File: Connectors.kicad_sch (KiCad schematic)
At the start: 13 parts, among them J11 Micro_SD_Card_Det, J12 JST-PH, J13 USB_C_Receptacle_USB2.0, U10 USBLC6-2SC6

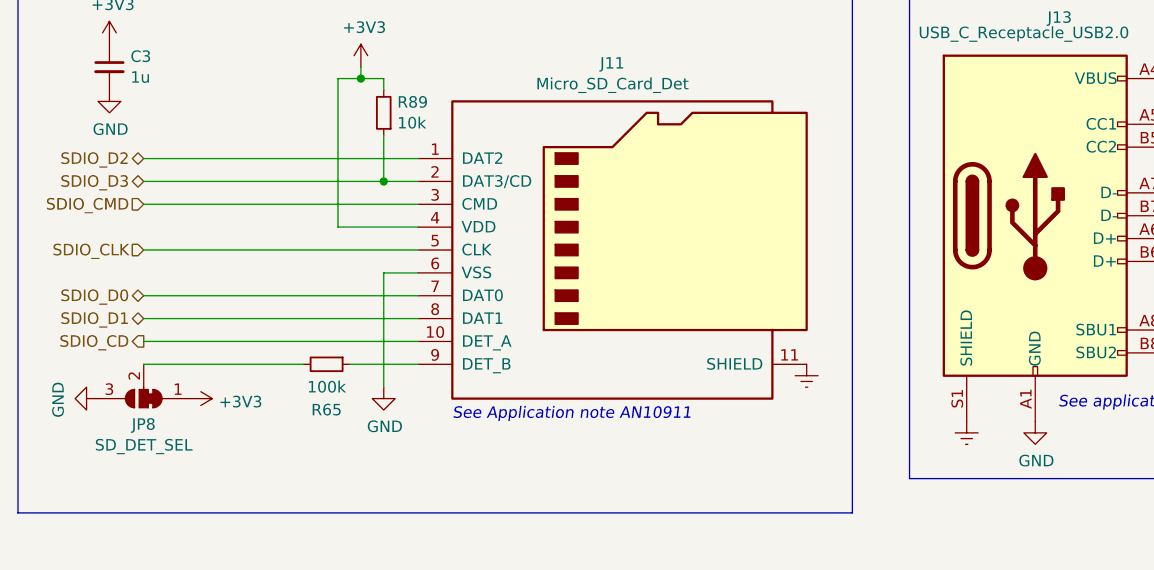
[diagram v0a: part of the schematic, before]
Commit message: (deps) upgrade to KiCad 7.0
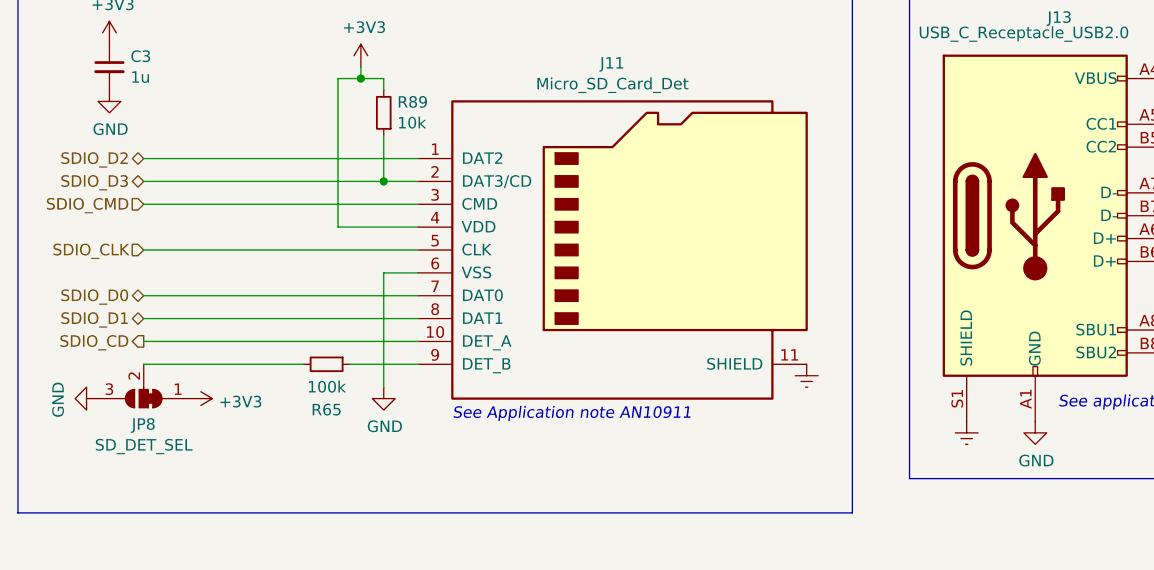
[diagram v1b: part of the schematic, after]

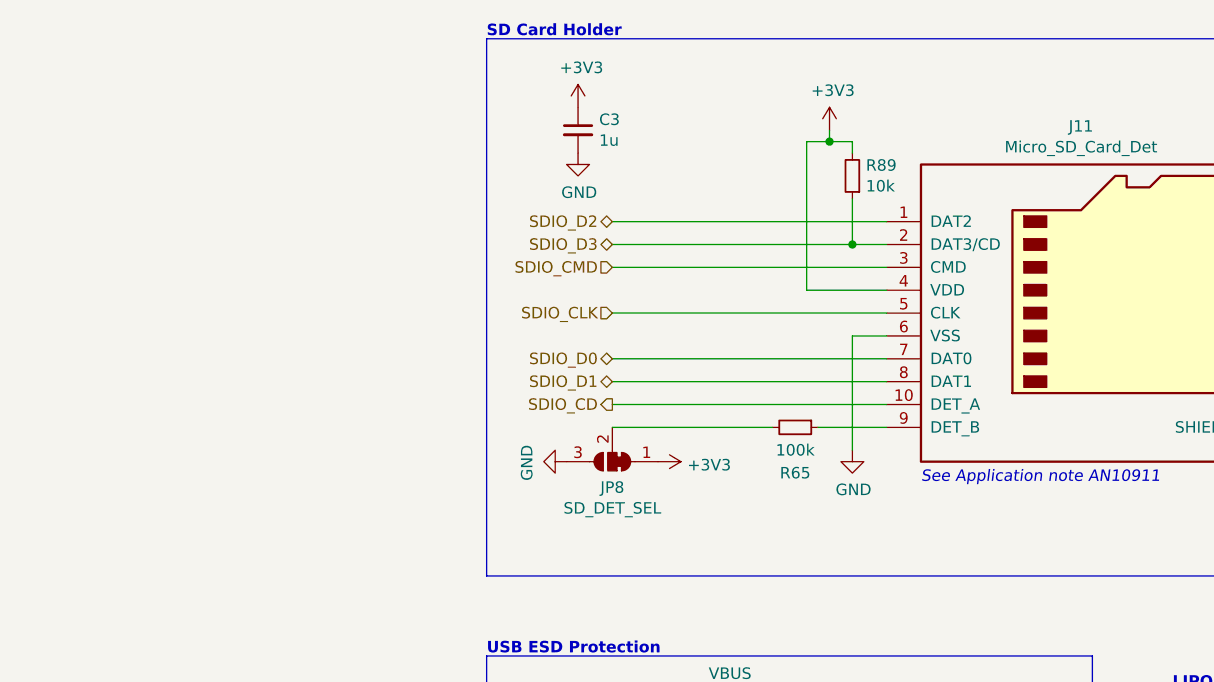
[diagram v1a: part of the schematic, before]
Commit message: (sch) update sd card interface
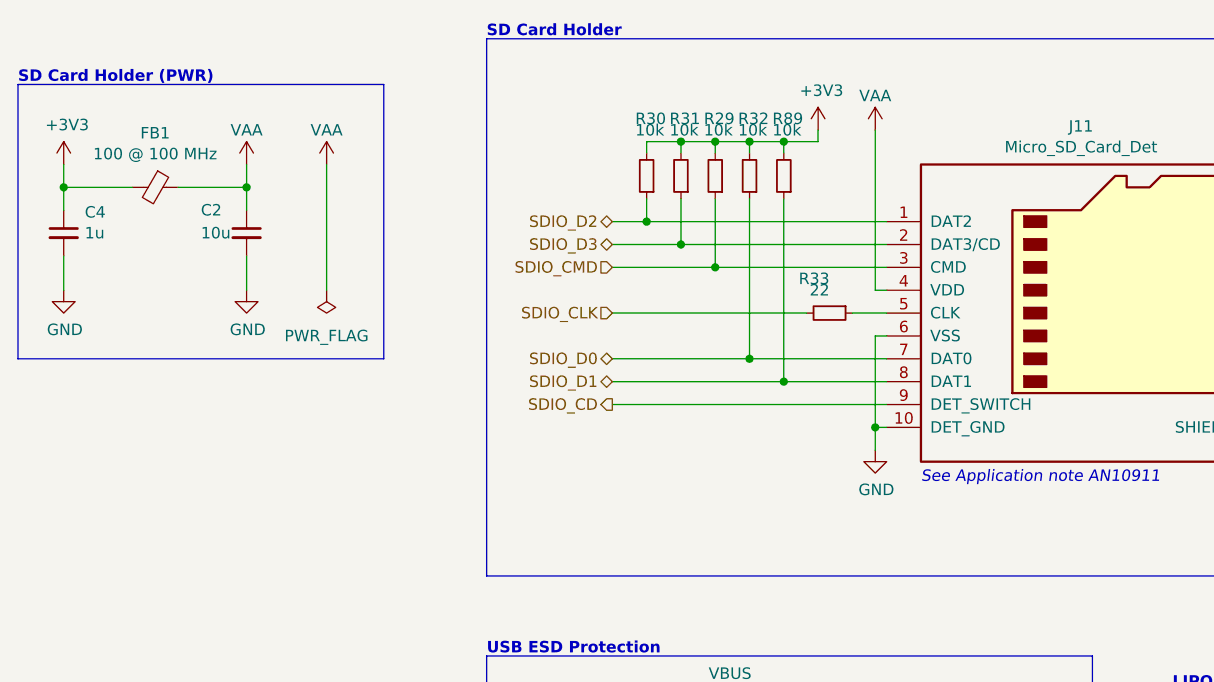
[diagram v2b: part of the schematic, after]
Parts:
- removed C3: 1u, Capacitor_SMD:C_0603_1608Metric_Pad1.08x0.95mm_HandSolder, symbol Device:C_Small
- removed JP8: SD_DET_SEL, Jumper:SolderJumper-3_P1.3mm_Bridged12_RoundedPad1.0x1.5mm_NumberLabels, symbol Jumper:SolderJumper_3_Bridged12
- removed R65: 100k, Resistor_SMD:R_0603_1608Metric_Pad0.98x0.95mm_HandSolder, symbol Device:R_Small
- added C2: 10u, Capacitor_SMD:C_0805_2012Metric_Pad1.18x1.45mm_HandSolder, symbol Device:C_Small
- added C4: 1u, Capacitor_SMD:C_0603_1608Metric_Pad1.08x0.95mm_HandSolder, symbol Device:C_Small
- added FB1: BLM18KG101TZ1D, Inductor_SMD:L_0603_1608Metric_Pad1.05x0.95mm_HandSolder, symbol Device:Ferrite_Bead_Small
- added R29, R30, R31, R32: 10k, Resistor_SMD:R_0603_1608Metric_Pad0.98x0.95mm_HandSolder, symbol Device:R_Small
- added R33: 22, Resistor_SMD:R_0603_1608Metric_Pad0.98x0.95mm_HandSolder, symbol Device:R_Small
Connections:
- net +3V3: now also C4.1, FB1.2, R29.2, R30.2, R31.2, R32.2; no longer J11.4 (VDD)
- net GND: now also J11.10 (DET_GND), C2.2, C4.2
- net SDIO_CD: now also J11.9 (DET_SWITCH); no longer J11.10 (DET_A)
- net SDIO_CLK: now also R33.2; no longer J11.5 (CLK)
- net SDIO_CMD: now also R29.1
- net SDIO_D0: now also R32.1
- net SDIO_D1: now also R89.1
- net SDIO_D2: now also R30.1
- net SDIO_D3: now also R31.1; no longer R89.1
- new net: J11.5 (CLK), R33.1
- new net VAA: C2.1, FB1.1, J11.4 (VDD)
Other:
- note added: "SD Card Holder (PWR)"
- moved on the sheet: R89

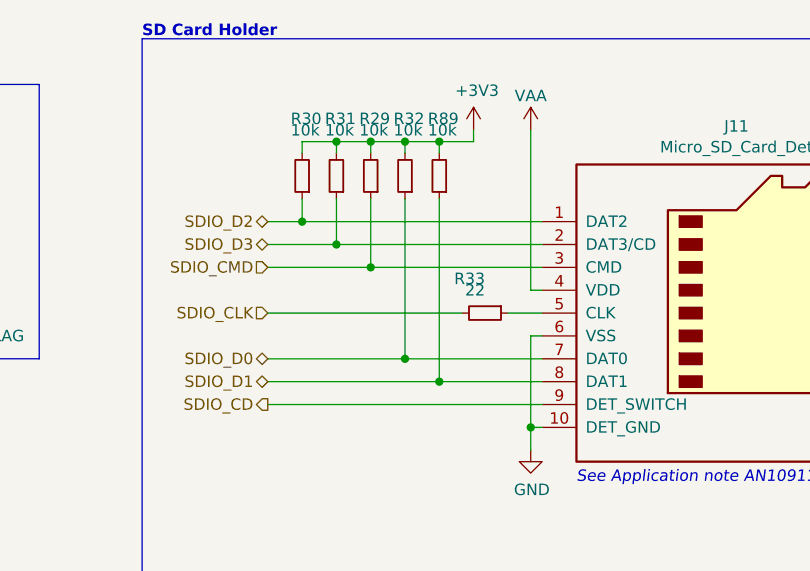
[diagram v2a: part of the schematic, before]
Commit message: (sch) update usr button to trigger boot0
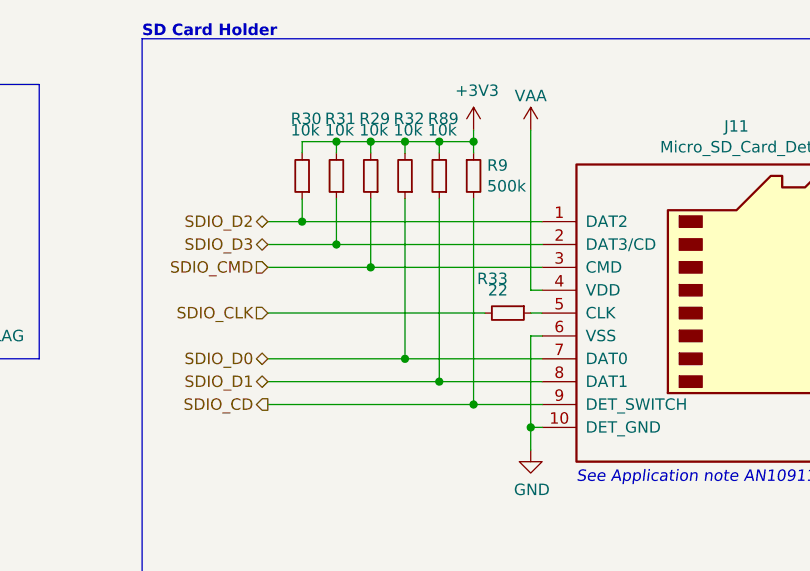
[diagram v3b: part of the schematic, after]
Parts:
- added R9: 500k, Resistor_SMD:R_0603_1608Metric_Pad0.98x0.95mm_HandSolder, symbol Device:R_Small
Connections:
- net +3V3: now also R9.1
- net SDIO_CD: now also R9.2
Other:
- moved on the sheet: R33
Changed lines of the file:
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@@
   (junction (at 91.44 74.93) (diameter 0) (color 0 0 0 0)
   )
+  (junction (at 106.68 63.5) (diameter 0) (color 0 0 0 0)
+  )
   (junction (at 102.87 63.5) (diameter 0) (color 0 0 0 0)
   )
@@
   )
   (junction (at 22.86 68.58) (diameter 0) (color 0 0 0 0)
+  )
+  (junction (at 106.68 92.71) (diameter 0) (color 0 0 0 0)
   )
   (junction (at 91.44 63.5) (diameter 0) (color 0 0 0 0)
@@
     (stroke (width 0) (type default))
   )
-  (wire (pts (xy 83.82 82.55) (xy 105.41 82.55))
+  (wire (pts (xy 83.82 82.55) (xy 107.95 82.55))
     (stroke (width 0) (type default))
   )
@@
     (stroke (width 0) (type default))
   )
-  (wire (pts (xy 110.49 82.55) (xy 114.3 82.55))
-    (stroke (width 0) (type default))
-  )
-  (wire (pts (xy 83.82 92.71) (xy 114.3 92.71))
+  (wire (pts (xy 113.03 82.55) (xy 114.3 82.55))
+    (stroke (width 0) (type default))
+  )
+  (wire (pts (xy 83.82 92.71) (xy 106.68 92.71))
     (stroke (width 0) (type default))
   )
@@
     (stroke (width 0) (type default))
   )
+  (wire (pts (xy 106.68 92.71) (xy 114.3 92.71))
+    (stroke (width 0) (type default))
+  )
   (wire (pts (xy 83.82 72.39) (xy 87.63 72.39))
     (stroke (width 0) (type default))
@@
     (stroke (width 0) (type default))
   )
+  (wire (pts (xy 106.68 63.5) (xy 106.68 64.77))
+    (stroke (width 0) (type default))
+  )
   (wire (pts (xy 152.4 137.16) (xy 152.4 132.08))
+    (stroke (width 0) (type default))
+  )
+  (wire (pts (xy 106.68 69.85) (xy 106.68 92.71))
     (stroke (width 0) (type default))
   )
@@
     )
   )
-  (symbol (lib_id "Device:R_Small") (at 107.95 82.55 270) (unit 1)
-    (in_bom yes) (on_board yes) (dnp no)
-    (property "Reference" "R33" (at 107.95 78.74 90)
+  (symbol (lib_id "Device:R_Small") (at 106.68 67.31 0) (unit 1)
+    (in_bom yes) (on_board yes) (dnp no)
+    (property "Reference" "R9" (at 108.1786 66.1416 0)
+      (effects (font (size 1.27 1.27)) (justify left))
+    )
+    (property "Value" "500k" (at 108.1786 68.453 0)
+      (effects (font (size 1.27 1.27)) (justify left))
+    )
+    (property "Footprint" "Resistor_SMD:R_0603_1608Metric_Pad0.98x0.95mm_HandSolder" (at 106.68 67.31 0)
+      (effects (font (size 1.27 1.27)) hide)
+    )
+    (property "Datasheet" "~" (at 106.68 67.31 0)
+      (effects (font (size 1.27 1.27)) hide)
+    )
+    (property "MPN" "RC0603FR-07470KL" (at 106.68 67.31 0)
+      (effects (font (size 1.27 1.27)) hide)
+    )
+    (property "Mfr." "Yageo" (at 106.68 67.31 0)
+      (effects (font (size 1.27 1.27)) hide)
+    )
+    (pin "1")
+    (pin "2")
+    (instances
+      (project "kleinvoet"
+        (path "/4185c36c-c66e-4dbd-be5d-841e551f4885"
+          (reference "R9") (unit 1)
+        )
+        (path "/4185c36c-c66e-4dbd-be5d-841e551f4885/00000000-0000-0000-0000-00005ef53a66"
+          (reference "R34") (unit 1)
+        )
+      )
+    )
+  )
+  (symbol (lib_id "Device:R_Small") (at 110.49 82.55 270) (unit 1)
+    (in_bom yes) (on_board yes) (dnp no)
+    (property "Reference" "R33" (at 110.49 78.74 90)
       (effects (font (size 1.27 1.27)) (justify right))
     )
-    (property "Value" "22" (at 107.95 80.01 90)
+    (property "Value" "22" (at 110.49 80.01 90)
       (effects (font (size 1.27 1.27)) (justify right))
     )
-    (property "Footprint" "Resistor_SMD:R_0603_1608Metric_Pad0.98x0.95mm_HandSolder" (at 107.95 82.55 0)
-      (effects (font (size 1.27 1.27)) hide)
-    )
-    (property "Datasheet" "~" (at 107.95 82.55 0)
-      (effects (font (size 1.27 1.27)) hide)
-    )
-    (property "MPN" "" (at 107.95 82.55 0)
-      (effects (font (size 1.27 1.27)) hide)
-    )
-    (property "Mfr." "Yageo" (at 107.95 82.55 0)
-      (effects (font (size 1.27 1.27)) hide)
-    )
+    (property "Footprint" "Resistor_SMD:R_0603_1608Metric_Pad0.98x0.95mm_HandSolder" (at 110.49 82.55 0)
+      (effects (font (size 1.27 1.27)) hide)
+    )
+    (property "Datasheet" "~" (at 110.49 82.55 0)
+      (effects (font (size 1.27 1.27)) hide)
+    )
+    (property "MPN" "" (at 110.49 82.55 0)
+      (effects (font (size 1.27 1.27)) hide)
+    )
+    (property "Mfr." "Yageo" (at 110.49 82.55 0)
+      (effects (font (size 1.27 1.27)) hide)
+    )

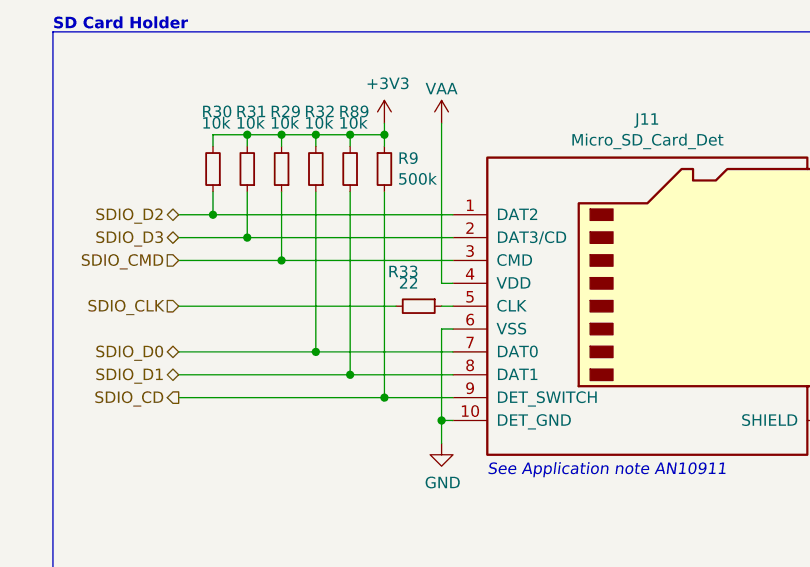
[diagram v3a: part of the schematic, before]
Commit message: (sch) change termination resistor
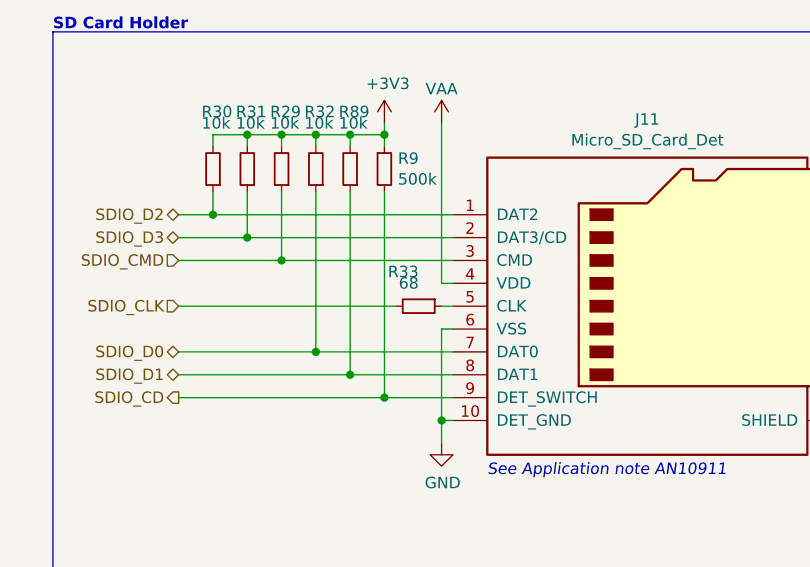
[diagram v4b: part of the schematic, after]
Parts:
- R33: value 22 -> 68
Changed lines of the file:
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@@
       (effects (font (size 1.27 1.27)) (justify right))
     )
-    (property "Value" "22" (at 110.49 80.01 90)
+    (property "Value" "68" (at 110.49 80.01 90)
       (effects (font (size 1.27 1.27)) (justify right))
     )
